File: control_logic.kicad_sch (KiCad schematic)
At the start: 59 parts, among them J12 SWD Header, J17 TC2050, SW1 TS342A2P, SW2 TS342A2P, U10 L7805, U11 MCP2562-E-SN, U12 STM32F105RCTx, U13 AZ1117I-3.3, U15 TPD4E1U06, Y3 8MHz 12pF

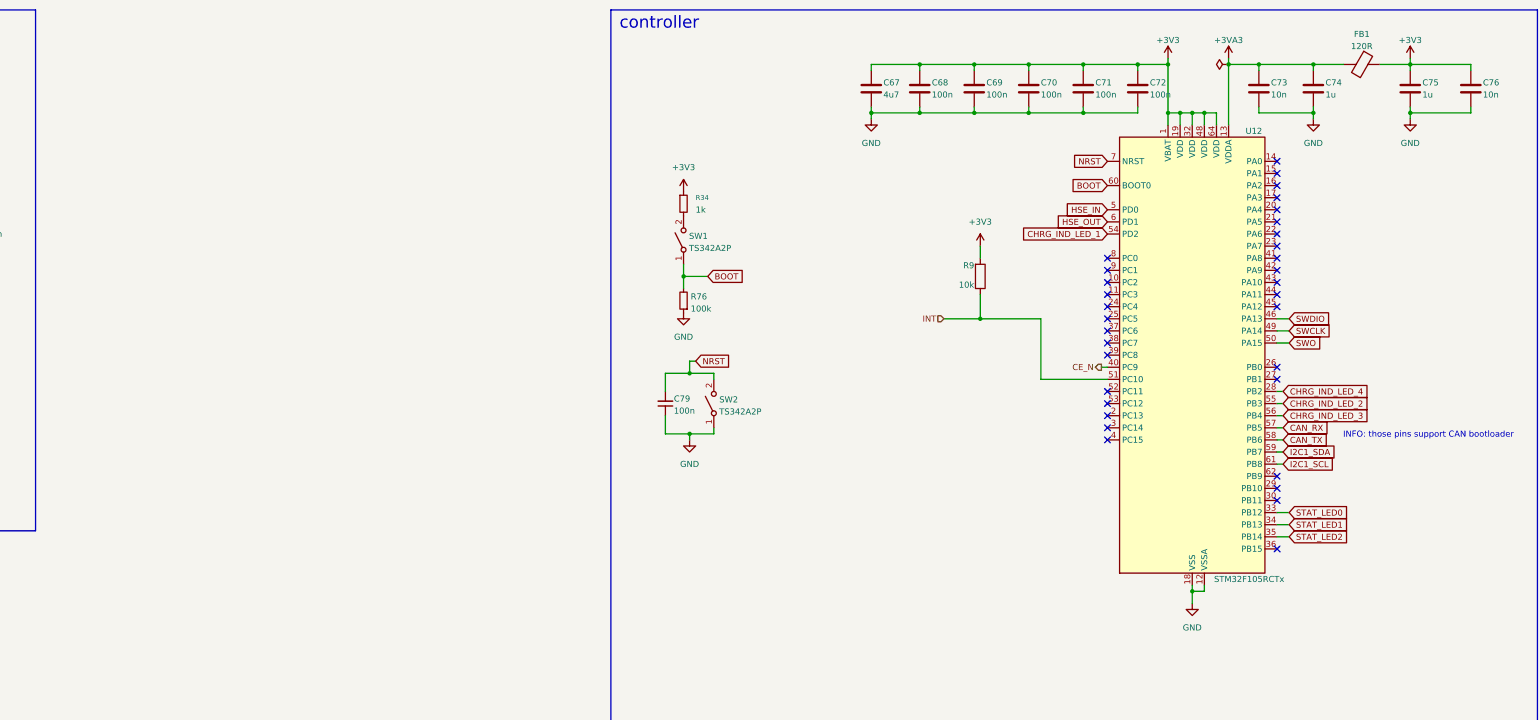
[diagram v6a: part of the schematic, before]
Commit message: adding voltage and current sensing capabilities. WIP
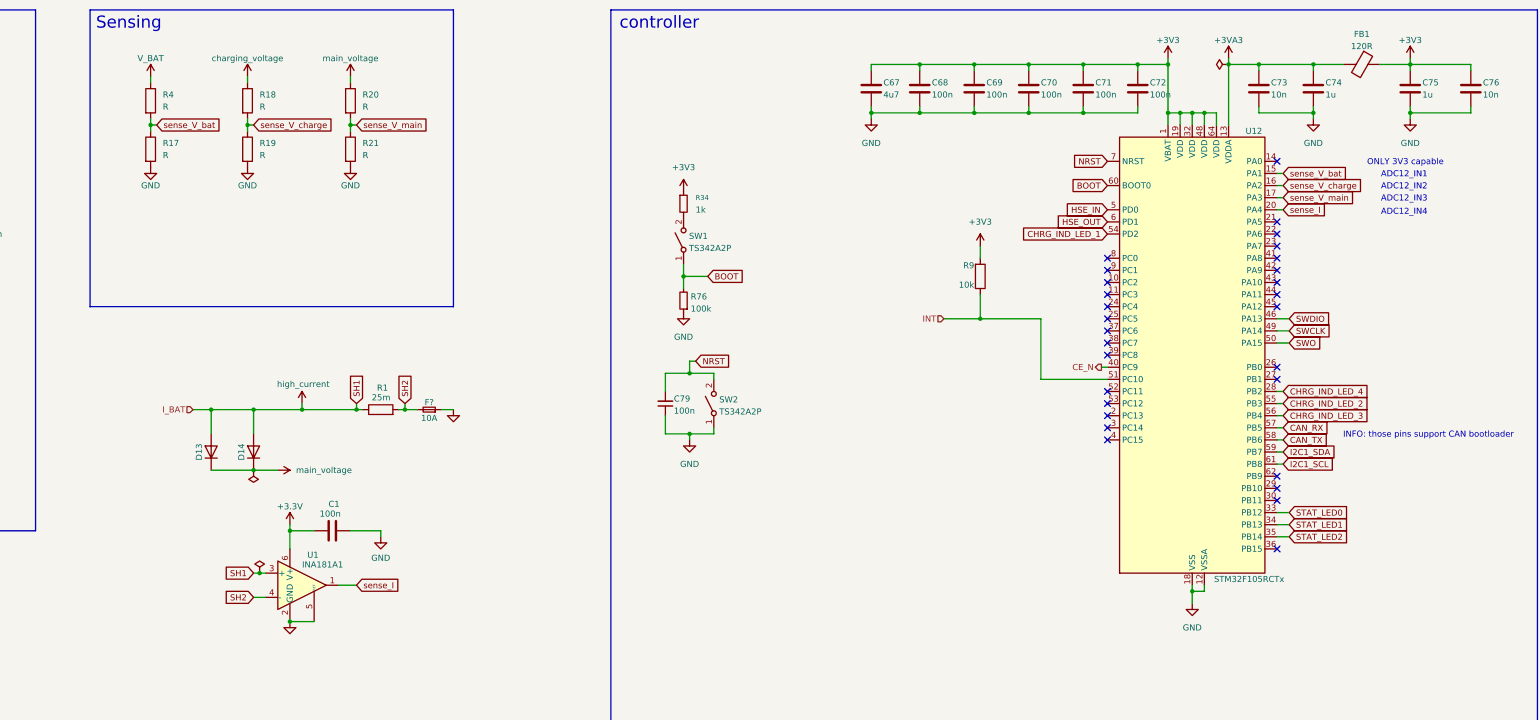
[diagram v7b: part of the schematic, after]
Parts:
- added C1: 100n, Capacitor_SMD:C_0402_1005Metric, symbol Device:C
- added D13, D14: D, Diode_SMD:D_SOD-123F, symbol Device:D
- added F?: 10A, Fuse:Fuse_1206_3216Metric, symbol Device:Fuse_Small
- added R1: 25m, Resistor_SMD:R_1206_3216Metric_Pad1.30x1.75mm_HandSolder, symbol Device:R
- added R17, R18, R19, R20, R21, R4: R, symbol Device:R
- added U1: INA181A1, Package_TO_SOT_SMD:SOT-23-6, symbol Amplifier_Current:INA181
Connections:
- net GND: now also C1.2, F?.1, R17.2, R19.2, R21.2, U1.2 (GND), U1.5 (REF)
- net charging_voltage: now also R18.1
- net main_voltage: now also D13.1 (K), D14.1 (K), R20.1
- net sense_V_bat: now reaches U12.15 (PA1)
- net sense_V_bat: now also R17.1, R4.2
- net sense_V_charge: now reaches U12.16 (PA2)
- net sense_V_charge: now also R18.2, R19.1
- net sense_V_main: now reaches U12.17 (PA3)
- net sense_V_main: now also R20.2, R21.1
- net sense_I: now reaches U12.20 (PA4)
- net sense_I: now also U1.1
- new net +3.3V: C1.1, U1.6 (V+)
- new net SH2: F?.2, R1.2, U1.4 (-)
- new net V_BAT: R4.1
- new net high_current: D13.2 (A), D14.2 (A), R1.1, U1.3 (+)
- no-connect marks 33 -> 29
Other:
- note added: "ADC12_IN1"
- note added: "ADC12_IN2"
- note added: "ADC12_IN3"
- note added: "ADC12_IN4"
- note added: "ONLY 3V3 capable"
- note added: "Sensing"

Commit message: calculated sensing-resistor values
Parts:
- R18: value R -> 68k; footprint (none) -> Resistor_SMD:R_0603_1608Metric; LCSC (none) -> C23231
- R19, R21: value R -> 10k; footprint (none) -> Resistor_SMD:R_0402_1005Metric; LCSC (none) -> C25744
- R20: value R -> 30k; footprint (none) -> Resistor_SMD:R_0603_1608Metric; LCSC (none) -> C22984
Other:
- note added: "12,6V"
- note added: "24V"
- note added: "V_CH_s/24V = R19/(R18+R19) V_CH_s_max = 3v3; R19 = 10k -> R18 ~ 68k"
- note added: "V_SNS/12.6V = R21/(R20+R21) V_SNS_max = 3v3; R21 = 10k -> R20 = 30k"
- moved on the sheet: R17, R18, R19, R4
